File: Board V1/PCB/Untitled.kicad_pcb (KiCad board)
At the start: 2 copper layers, 13 parts, among them U1 MCP2515-xSO, U2 LM78L05_SO8, Y1 16MHz

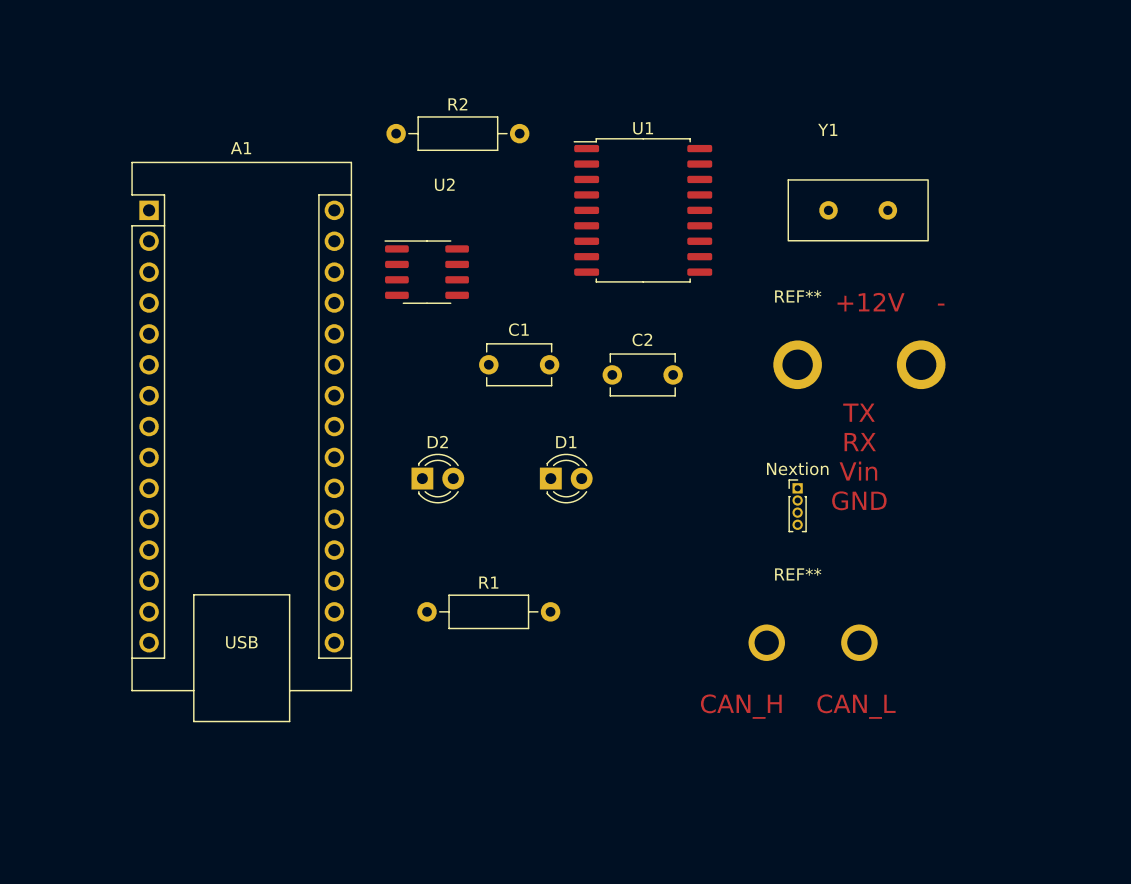
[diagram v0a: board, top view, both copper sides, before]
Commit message: Added new version of board with correct can chips
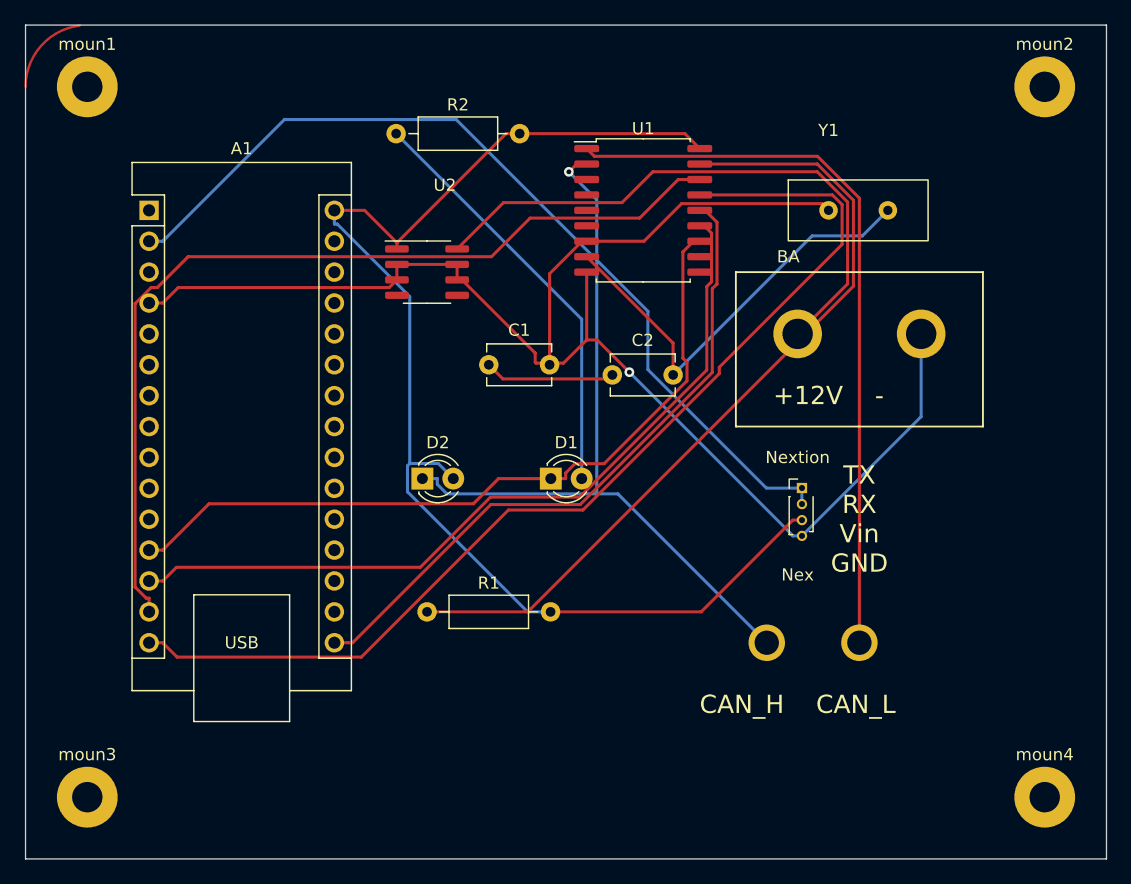
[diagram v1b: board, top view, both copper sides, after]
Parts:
- added moun1: MountingHole_2.5mm_Pad, MountingHole:MountingHole_2.5mm_Pad, F.Cu at (17.8, 17.8)
- added moun2: MountingHole_2.5mm_Pad, MountingHole:MountingHole_2.5mm_Pad, F.Cu at (96.5, 17.8)
- added moun3: MountingHole_2.5mm_Pad, MountingHole:MountingHole_2.5mm_Pad, F.Cu at (17.8, 76.2)
- added moun4: MountingHole_2.5mm_Pad, MountingHole:MountingHole_2.5mm_Pad, F.Cu at (96.5, 76.2)
- Nextion: value PinHeader_1x04_P1.00mm_Vertical -> PinHeader_1x04_P200mm_Vertical
- moved BA 2.54 mm to (76.2, 33.0)
- renumbered REF** to BA, REF** to Nex
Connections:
- C2 pad 2: Net-(C1-Pad2) -> Net-(C2-Pad2)
- Nextion pad 2: Nex TX -> Nex RX
- U1 pad 8: Net-(C1-Pad2) -> Net-(C2-Pad2)
- Y1 pad 2: Net-(C1-Pad2) -> Net-(C2-Pad2)
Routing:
- net Vdd: track 0.00 -> 105.6 mm
- net Vss: track 0.00 -> 94.0 mm, vias 0 -> 1
- net Net-(A1-Pad15): track 0.00 -> 87.2 mm
- net Net-(A1-Pad14): track 0.00 -> 76.6 mm
- net Nex RX: track 0.00 -> 74.5 mm
- net Net-(R1-Pad1): track 0.00 -> 67.1 mm
- net Net-(A1-Pad13): track 0.00 -> 65.7 mm
- net Can High: track 0.00 -> 63.3 mm, vias 0 -> 1
- net Net-(A1-Pad12): track 0.00 -> 62.8 mm
- net Can Low: track 0.00 -> 60.7 mm
- net Net-(A1-Pad16): track 0.00 -> 54.6 mm
- net Vin: track 0.00 -> 48.3 mm
- net Net-(C2-Pad2): track 0.00 -> 35.9 mm
- net Net-(D1-Pad2): track 0.00 -> 34.7 mm
- net Net-(C1-Pad2): track 0.00 -> 33.0 mm
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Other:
- board outline added: 88.9 x 68.6 mm
